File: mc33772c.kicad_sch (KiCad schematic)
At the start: 0 parts

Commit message: feat: STM32F446RE basically done, MC33772C remains
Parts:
- added U2: MC33772CTP1AE, Package_QFP:LQFP-48-1EP_7x7mm_P0.5mm_EP3.6x3.6mm, symbol mc33772c:MC33772CTP1AE
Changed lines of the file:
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@@
 	(generator_version "10.0")
 	(paper "A4")
+	(symbol
+		(lib_id "mc33772c:MC33772CTP1AE")
+		(at 238.76 100.33 0)
+		(unit 1)
+		(body_style 1)
+		(exclude_from_sim no)
+		(in_bom yes)
+		(on_board yes)
+		(in_pos_files yes)
+		(dnp no)
+		(fields_autoplaced yes)
+		(property "Reference" "U2"
+			(at 269.24 82.8292 0)
+			(show_name no)
+			(do_not_autoplace no)
+			(effects
+				(font
+					(size 1.27 1.27)
+				)
+			)
+		)
+		(property "Value" "MC33772CTP1AE"
+			(at 269.24 85.3692 0)
+			(show_name no)
+			(do_not_autoplace no)
+			(effects
+				(font
+					(size 1.27 1.27)
+				)
+			)
+		)
+		(property "Footprint" "Package_QFP:LQFP-48-1EP_7x7mm_P0.5mm_EP3.6x3.6mm"
+			(at 223.266 148.082 0)
+			(hide yes)
+			(show_name no)
+			(do_not_autoplace no)
+			(effects
+				(font
+					(size 1.27 1.27)
+				)
+				(justify right)
+			)
+		)
+		(property "Datasheet" "https://www.nxp.com/docs/en/data-sheet/MC33772C-DS.pdf"
+			(at 214.122 154.178 0)
+			(hide yes)
+			(show_name no)
+			(do_not_autoplace no)
+			(effects
+				(font
+					(size 1.27 1.27)
+				)
+			)
+		)
+		(property "Description" ""
+			(at 234.188 151.13 0)
+			(hide yes)
+			(show_name no)
+			(do_not_autoplace no)
+			(effects
+				(font
+					(size 1.27 1.27)
+				)
+			)
+		)
+		(pin "3"
+		)
+		(pin "4"
+		)
+		(pin "1"
+		)
+		(pin "6"
+		)
+		(pin "2"
+		)
+		(pin "5"
+		)
+		(pin "10"
+		)
+		(pin "8"
+		)
+		(pin "9"
+		)
+		(pin "7"
+		)
+		(pin "11"
+		)
+		(pin "36"
+		)
+		(pin "37"
+		)
+		(pin "38"
+		)
+		(pin "39"
+		)
+		(pin "40"
+		)
+		(pin "41"
+		)
+		(pin "42"
+		)
+		(pin "43"
+		)
+		(pin "44"
+		)
+		(pin "45"
+		)
+		(pin "46"
+		)
+		(pin "47"
+		)
+		(pin "48"
+		)
+		(pin "49"
+		)
+		(pin "14"
+		)
+		(pin "13"
+		)
+		(pin "12"
+		)
+		(pin "24"
+		)
+		(pin "23"
+		)
+		(pin "22"
+		)
+		(pin "21"
+		)
+		(pin "29"
+		)
+		(pin "30"
+		)
+		(pin "31"
+		)
+		(pin "32"
+		)
+		(pin "33"
+		)
+		(pin "34"
+		)
+		(pin "35"
+		)
+		(pin "20"
+		)
+		(pin "15"
+		)
+		(pin "16"
+		)
+		(pin "17"
+		)
+		(pin "18"
+		)
+		(pin "19"
+		)
+		(pin "28"
+		)
+		(pin "27"
+		)
+		(pin "26"
+		)
+		(pin "25"
+		)
+		(instances
+			(project "stm32f446re-mc33772c"
+				(path "/d1dd5335-1fc0-4e41-b998-ab2aec4b6fde"
+					(reference "U2")
+					(unit 1)
+				)
+			)
+		)
+	)
 	(sheet_instances
 		(path "/"

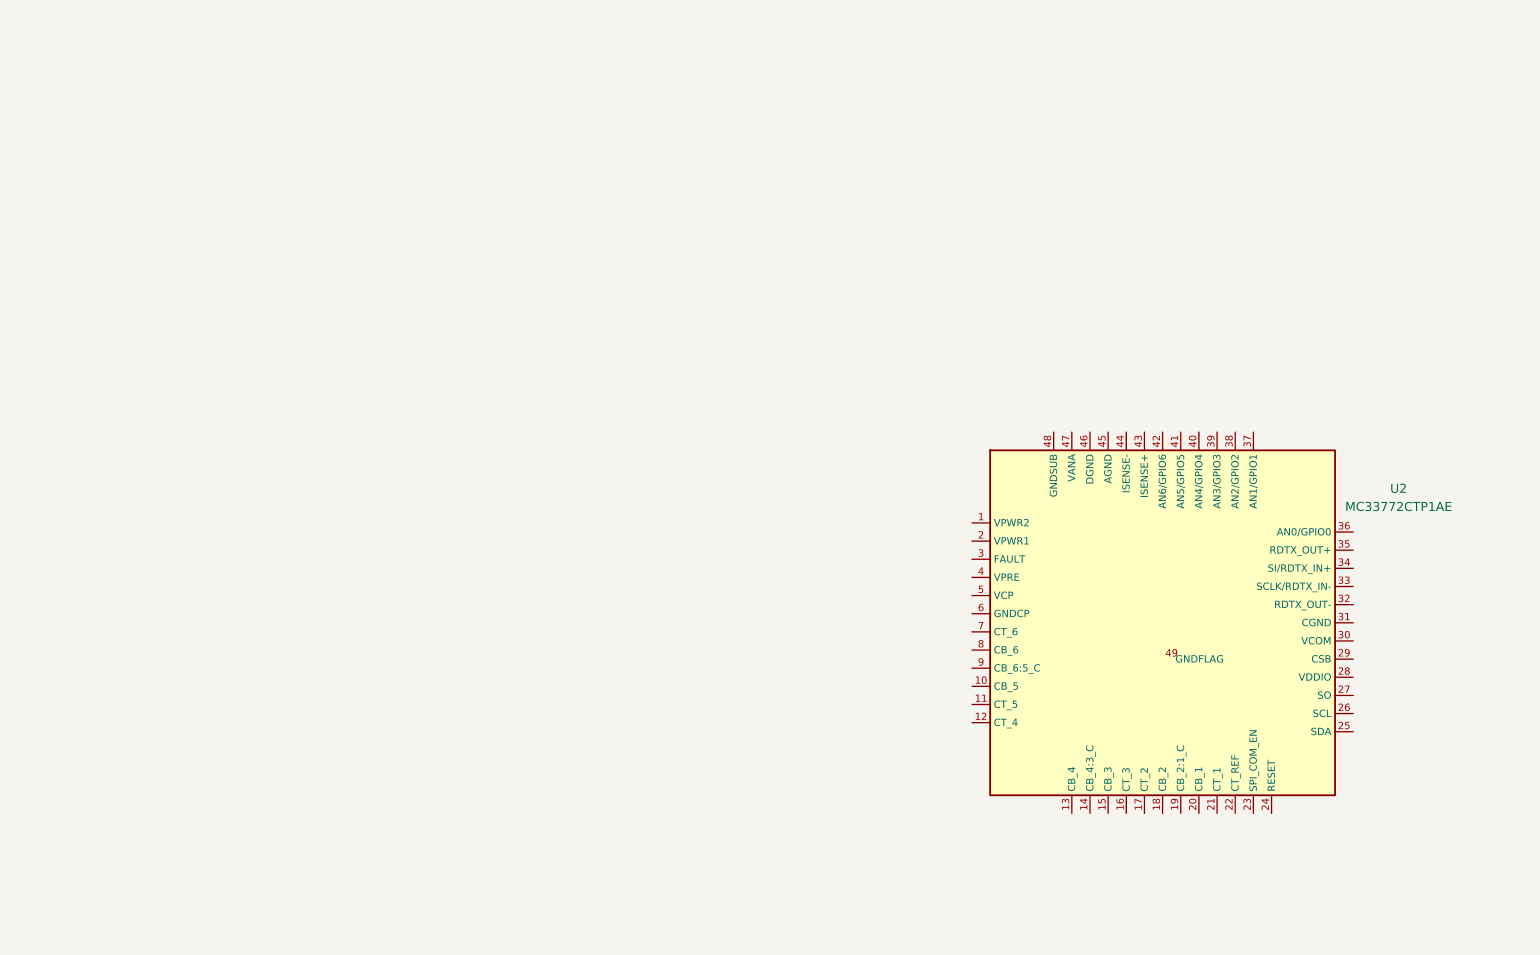
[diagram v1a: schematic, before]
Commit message: MC33772C basically done. connector need update.
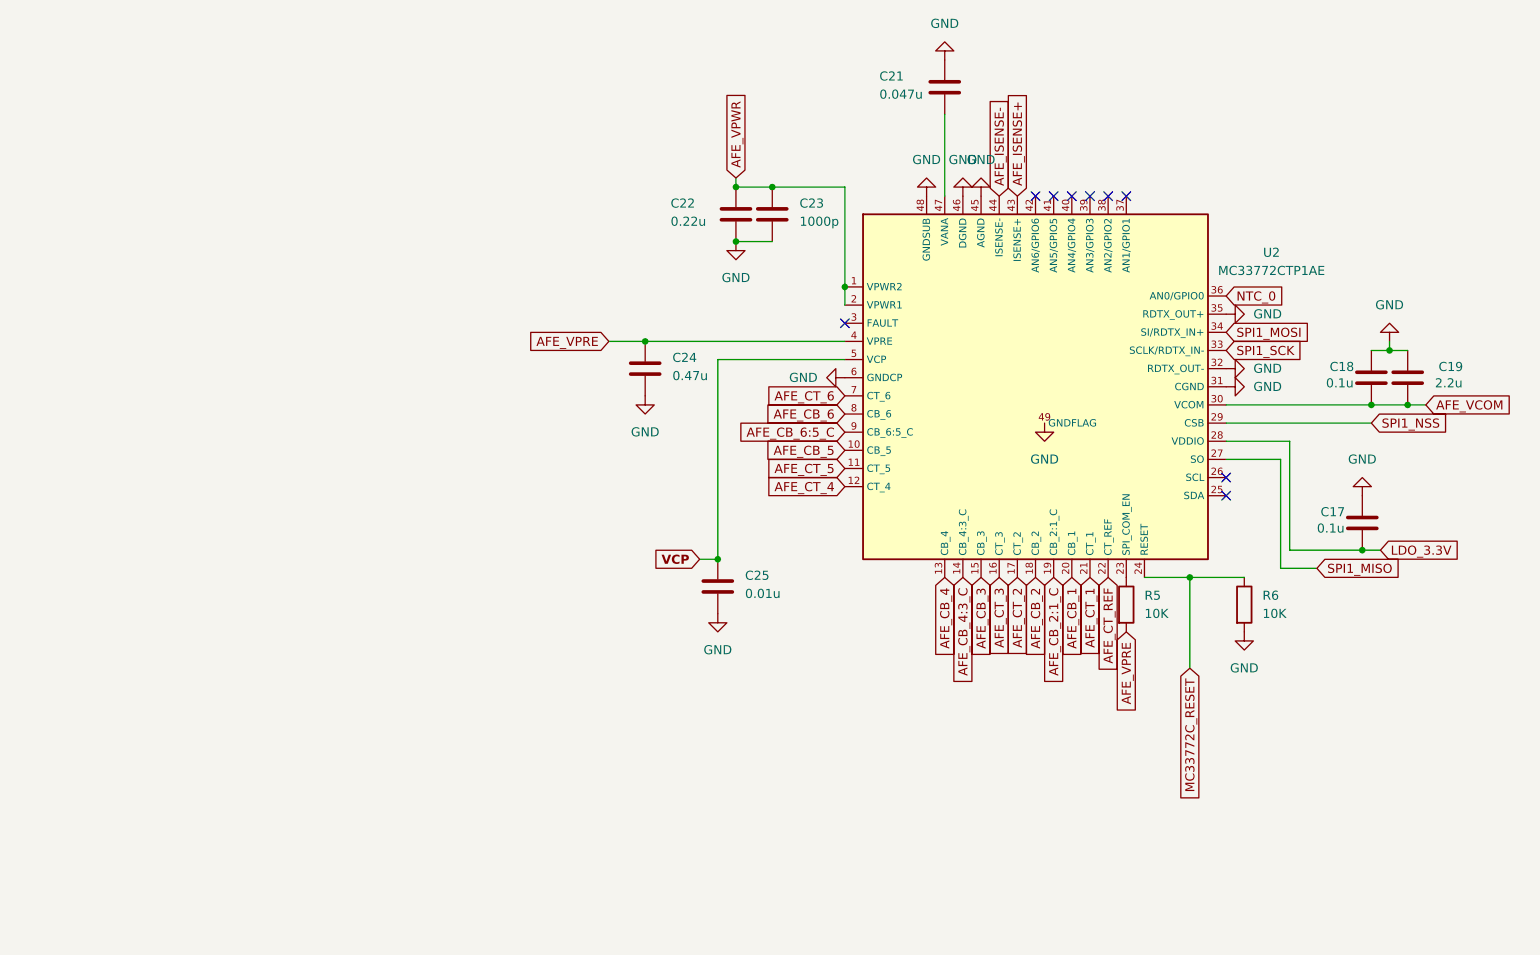
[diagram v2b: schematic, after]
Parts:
- added C17, C18: 0.1u, symbol Device:C
- added C19: 2.2u, symbol Device:C
- added C21: 0.047u, symbol Device:C
- added C22: 0.22u, symbol Device:C
- added C23: 1000p, symbol Device:C
- added C24: 0.47u, symbol Device:C
- added C25: 0.01u, symbol Device:C
- added R5, R6: 10K, symbol Device:R
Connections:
- net AFE_VPWR: now reaches U2.1 (VPWR2)
- net AFE_VPWR: now also U2.2 (VPWR1), C22.1, C23.1
- net AFE_CB_5: now reaches U2.10 (CB_5)
- net AFE_CT_5: now reaches U2.11 (CT_5)
- net AFE_CT_4: now reaches U2.12 (CT_4)
- net AFE_CB_4: now reaches U2.13 (CB_4)
- net AFE_CB_4:3_C: now reaches U2.14 (CB_4:3_C)
- net AFE_CB_3: now reaches U2.15 (CB_3)
- net AFE_CT_3: now reaches U2.16 (CT_3)
- net AFE_CT_2: now reaches U2.17 (CT_2)
- net AFE_CB_2: now reaches U2.18 (CB_2)
- net AFE_CB_2:1_C: now reaches U2.19 (CB_2:1_C)
- net AFE_CB_1: now reaches U2.20 (CB_1)
- net AFE_CT_1: now reaches U2.21 (CT_1)
- net AFE_CT_REF: now reaches U2.22 (CT_REF)
- net at U2.23 (SPI_COM_EN): now also R5.1
- net MC33772C_RESET: now reaches U2.24 (RESET)
- net MC33772C_RESET: now also R6.1
- net SPI1_MISO: now reaches U2.27 (SO)
- net LDO_3.3V: now reaches U2.28 (VDDIO)
- net LDO_3.3V: now also C17.2
- net SPI1_NSS: now reaches U2.29 (CSB)
- net AFE_VCOM: now reaches U2.30 (VCOM)
- net AFE_VCOM: now also C18.2, C19.2
- net GND: now reaches U2.31 (CGND)
- net GND: now also U2.32 (RDTX_OUT-), U2.35 (RDTX_OUT+), U2.45 (AGND), U2.46 (DGND), U2.48 (GNDSUB), U2.49 (GNDFLAG), U2.6 (GNDCP), C17.1, C18.1, C19.1, C21.1, C22.2, C23.2, C24.2, C25.2, R6.2
- net SPI1_SCK: now reaches U2.33 (SCLK/RDTX_IN-)
- net SPI1_MOSI: now reaches U2.34 (SI/RDTX_IN+)
- net NTC_0: now reaches U2.36 (AN0/GPIO0)
- net AFE_VPRE: now reaches U2.4 (VPRE)
- net AFE_VPRE: now also C24.1, R5.2
- net AFE_ISENSE+: now reaches U2.43 (ISENSE+)
- net AFE_ISENSE-: now reaches U2.44 (ISENSE-)
- net at U2.47 (VANA): now also C21.2
- net VCP: now reaches U2.5 (VCP)
- net VCP: now also C25.1
- net AFE_CT_6: now reaches U2.7 (CT_6)
- net AFE_CB_6: now reaches U2.8 (CB_6)
- net AFE_CB_6:5_C: now reaches U2.9 (CB_6:5_C)
- no-connect marks 0 -> 9
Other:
- moved on the sheet: U2

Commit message: schematic done
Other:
- moved on the sheet: C17, C18, C19, C21, C22, C23, C24, C25, R5, R6, U2

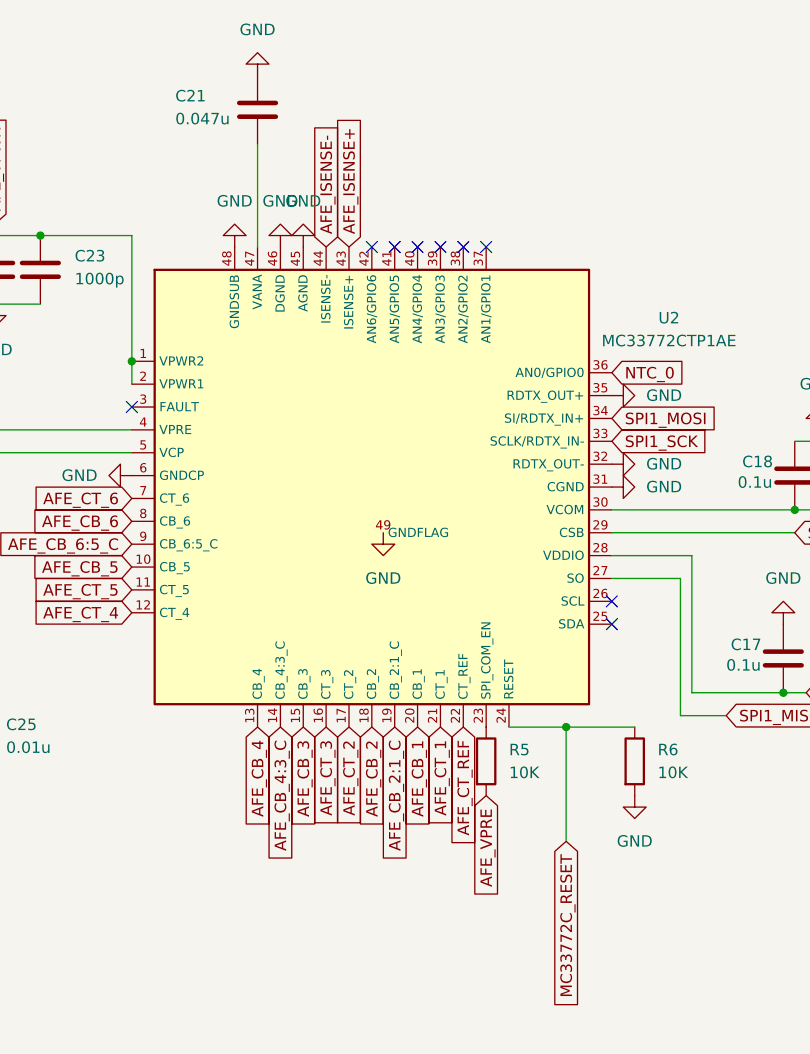
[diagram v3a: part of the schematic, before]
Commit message: fullup the annotation for update PCB from Schematics
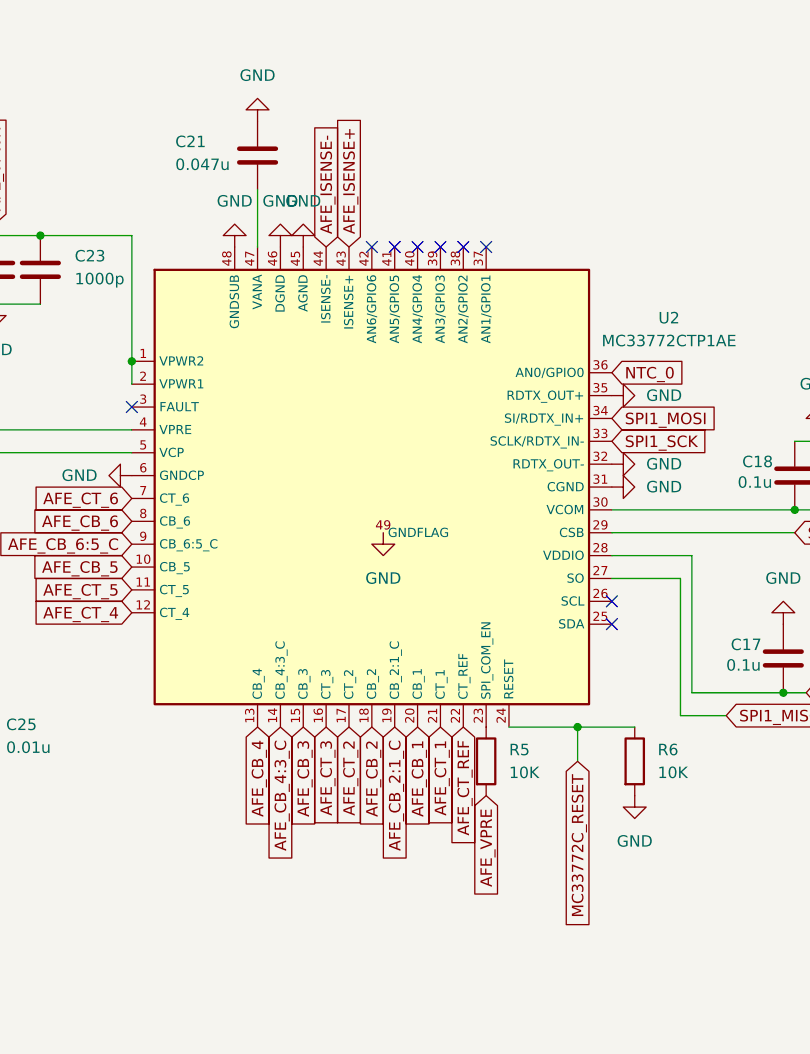
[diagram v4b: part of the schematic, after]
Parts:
- C17, C18, C21, C22, C23, C25: footprint (none) -> Capacitor_SMD:C_0402_1005Metric
- C19: footprint (none) -> Capacitor_SMD:C_0805_2012Metric
- C24: footprint (none) -> Capacitor_SMD:C_0603_1608Metric
- R5, R6: footprint (none) -> Resistor_SMD:R_0402_1005Metric
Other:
- moved on the sheet: C21
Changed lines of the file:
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@@
 	)
 	(junction
-		(at 93.98 78.74)
+		(at 171.45 111.76)
 		(diameter 0)
 		(color 0 0 0 0)
 	)
 	(junction
-		(at 195.58 87.63)
+		(at 93.98 78.74)
 		(diameter 0)
 		(color 0 0 0 0)
 	)
 	(junction
-		(at 104.14 109.22)
+		(at 195.58 87.63)
 		(diameter 0)
 		(color 0 0 0 0)
 	)
 	(junction
-		(at 106.68 64.77)
+		(at 104.14 109.22)
 		(diameter 0)
 		(color 0 0 0 0)
 	)
 	(junction
-		(at 170.18 111.76)
+		(at 106.68 64.77)
 		(diameter 0)
 		(color 0 0 0 0)
@@
 	(wire
 		(pts
-			(xy 135.89 46.99) (xy 135.89 58.42)
+			(xy 135.89 52.07) (xy 135.89 58.42)
 		)
 		(stroke
@@
 	(wire
 		(pts
-			(xy 170.18 111.76) (xy 163.83 111.76)
+			(xy 163.83 111.76) (xy 171.45 111.76)
 		)
 		(stroke
@@
 	(wire
 		(pts
-			(xy 170.18 111.76) (xy 177.8 111.76)
+			(xy 88.9 78.74) (xy 93.98 78.74)
 		)
 		(stroke
@@
 	(wire
 		(pts
-			(xy 88.9 78.74) (xy 93.98 78.74)
+			(xy 121.92 57.15) (xy 121.92 71.12)
 		)
 		(stroke
@@
 	(wire
 		(pts
-			(xy 121.92 57.15) (xy 121.92 71.12)
+			(xy 171.45 111.76) (xy 177.8 111.76)
 		)
 		(stroke
@@
 	(wire
 		(pts
-			(xy 170.18 111.76) (xy 170.18 124.46)
+			(xy 171.45 111.76) (xy 171.45 115.57)
 		)
 		(stroke
@@
 	(global_label "MC33772C_RESET"
 		(shape input)
-		(at 170.18 124.46 270)
+		(at 171.45 115.57 270)
 		(fields_autoplaced yes)
 		(effects
@@
 		)
 		(property "Intersheetrefs" "${INTERSHEET_REFS}"
-			(at 170.18 144.6728 90)
+			(at 171.45 135.7828 90)
 			(hide yes)
 			(show_name no)
@@
 			)
 		)
-		(property "Footprint" ""
+		(property "Footprint" "Capacitor_SMD:C_0805_2012Metric"
 			(at 201.6252 87.63 0)
 			(hide yes)
@@
 			)
 		)
-		(property "Datasheet" ""
+		(property "Datasheet" "https://pim.murata.com/asset/pim4/ceramicCapacitorSMD/GCM21BR71C225KA64-01A-EN_PDF_CERAMICCAPACITORSMD"
 			(at 200.66 83.82 0)
 			(hide yes)
@@
 			)
 		)
-		(property "Description" "Unpolarized capacitor"
+		(property "Description" "GCM21BR71C225KA64L"
 			(at 200.66 83.82 0)
 			(hide yes)
@@
 			)
 		)
-		(property "Footprint" ""
+		(property "Footprint" "Capacitor_SMD:C_0603_1608Metric"
 			(at 94.9452 86.36 0)
 			(hide yes)
@@
 			)
 		)
-		(property "Description" "Unpolarized capacitor"
+		(property "Description" "CAP CER 0.47uF 16V 10% X7R AEC-Q200 0603"
 			(at 93.98 82.55 0)
 			(hide yes)
@@
 			)
 		)
-		(property "Footprint" ""
+		(property "Footprint" "Resistor_SMD:R_0402_1005Metric"
 			(at 176.022 115.57 90)
 			(hide yes)
@@
 			)
 		)
-		(property "Datasheet" ""
+		(property "Datasheet" "https://www.mouser.tw/datasheet/3/508/1/PYu-RC_Group_51_RoHS_L_12.pdf"
 			(at 177.8 115.57 0)
 			(hide yes)
@@
 			)
 		)
-		(property "Description" "Resistor"
+		(property "Description" "RC0402FR-7D10KL"
 			(at 177.8 115.57 0)
 			(hide yes)
@@
 			)
 		)
-		(property "Footprint" ""
+		(property "Footprint" "Capacitor_SMD:C_0402_1005Metric"
 			(at 107.6452 64.77 0)
 			(hide yes)
@@
 			)
 		)
-		(property "Description" "Unpolarized capacitor"
+		(property "Description" "CAP CER 0.22uF 50V 10% X5R 0402"
 			(at 106.68 60.96 0)
 			(hide yes)
@@
 			)
 		)
-		(property "Footprint" ""
+		(property "Footprint" "Capacitor_SMD:C_0402_1005Metric"
 			(at 105.1052 116.84 0)
 			(hide yes)
@@
 			)
 		)
-		(property "Description" "Unpolarized capacitor"
+		(property "Description" "CAP CER 0.01uF 50V 10% X7R 0402"
 			(at 104.14 113.03 0)
 			(hide yes)
@@
 			)
 		)
-		(property "Footprint" ""
+		(property "Footprint" "Capacitor_SMD:C_0402_1005Metric"
 			(at 196.5452 87.63 0)
 			(hide yes)
@@
 			)
 		)
-		(property "Datasheet" ""
+		(property "Datasheet" "https://pim.murata.com/asset/pim4/ceramicCapacitorSMD/GCM155R71H104KE02-01A-EN_PDF_CERAMICCAPACITORSMD"
 			(at 195.58 83.82 0)
 			(hide yes)
@@
 			)
 		)
-		(property "Description" "Unpolarized capacitor"
+		(property "Description" "GCM155R71H104KE02J"
 			(at 195.58 83.82 0)
 			(hide yes)
@@
 			)
 		)
-		(property "Footprint" ""
+		(property "Footprint" "Capacitor_SMD:C_0402_1005Metric"
 			(at 195.2752 107.95 0)
 			(hide yes)
@@
 			)
 		)
-		(property "Datasheet" ""
+		(property "Datasheet" "https://pim.murata.com/asset/pim4/ceramicCapacitorSMD/GCM155R71H104KE02-01A-EN_PDF_CERAMICCAPACITORSMD"
 			(at 194.31 104.14 0)
 			(hide yes)
@@
 			)
 		)
-		(property "Description" "Unpolarized capacitor"
+		(property "Description" "GCM155R71H104KE02J"
 			(at 194.31 104.14 0)
 			(hide yes)
@@
 			)
 		)
-		(property "Footprint" ""
+		(property "Footprint" "Capacitor_SMD:C_0402_1005Metric"
 			(at 112.7252 64.77 0)
 			(hide yes)
@@
 			)
 		)
-		(property "Description" "Unpolarized capacitor"
+		(property "Description" "CAP CER 1000PF 50V 5% C0G 0402"
 			(at 111.76 60.96 0)
 			(hide yes)
@@
 	(symbol
 		(lib_id "power:GND")
-		(at 135.89 39.37 180)
+		(at 135.89 44.45 180)
 		(unit 1)
 		(body_style 1)
@@
 		(fields_autoplaced yes)
 		(property "Reference" "#PWR020"
-			(at 135.89 33.02 0)
+			(at 135.89 38.1 0)
 			(hide yes)
 			(show_name no)
@@
 		)
 		(property "Value" "GND"
-			(at 135.89 34.29 0)
+			(at 135.89 39.37 0)
 			(show_name no)
 			(do_not_autoplace no)
@@
 		)
 		(property "Footprint" ""
-			(at 135.89 39.37 0)
+			(at 135.89 44.45 0)
 			(hide yes)
 			(show_name no)
@@
 		)
 		(property "Datasheet" ""
-			(at 135.89 39.37 0)
+			(at 135.89 44.45 0)
 			(hide yes)
 			(show_name no)
@@
 		)
 		(property "Description" "Power symbol creates a global label with name \"GND\" , ground"
-			(at 135.89 39.37 0)
+			(at 135.89 44.45 0)
 			(hide yes)
 			(show_name no)
@@
 			)
 		)
-		(property "Footprint" ""
+		(property "Footprint" "Resistor_SMD:R_0402_1005Metric"
 			(at 159.512 115.57 90)
 			(hide yes)
@@
 			)
 		)
-		(property "Description" "Resistor"
+		(property "Description" "RES MF 10.0K 1/16W 1% AEC-Q200 0402"
 			(at 161.29 115.57 0)
 			(hide yes)
@@
 	(symbol
 		(lib_id "Device:C")
-		(at 135.89 43.18 0)
+		(at 135.89 48.26 0)
 		(unit 1)
 		(body_style 1)
@@
 		(dnp no)
 		(property "Reference" "C21"
-			(at 126.746 41.656 0)
+			(at 126.746 46.736 0)
 			(show_name no)
 			(do_not_autoplace no)
@@
 		)
 		(property "Value" "0.047u"
-			(at 126.746 44.196 0)
+			(at 126.746 49.276 0)
 			(show_name no)
 			(do_not_autoplace no)
@@
 			)
 		)
-		(property "Footprint" ""
-			(at 136.8552 46.99 0)
+		(property "Footprint" "Capacitor_SMD:C_0402_1005Metric"
+			(at 136.8552 52.07 0)
 			(hide yes)
 			(show_name no)
@@
 			)
 		)
-		(property "Datasheet" ""
-			(at 135.89 43.18 0)
+		(property "Datasheet" "https://mm.digikey.com/Volume0/opasdata/d220001/medias/docus/8942/490_Chip_Multilayer_CAT2021_MLCC.pdf"
+			(at 135.89 48.26 0)
 			(hide yes)
 			(show_name no)
@@
 			)
 		)
-		(property "Description" "Unpolarized capacitor"
-			(at 135.89 43.18 0)
+		(property "Description" "GRM155R71H473KE14D"
+			(at 135.89 48.26 0)
 			(hide yes)
 			(show_name no)
